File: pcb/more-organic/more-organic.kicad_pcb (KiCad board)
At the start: 2 copper layers, 156.4 x 122.7 mm, 66 parts, among them SW1 SW_Push, SW10 SW_Push, SW11 SW_Push, SW12 SW_Push, SW13 SW_Push, SW14 SW_Push, SW15 SW_Push, SW16 SW_Push, SW17 SW_Push, SW18 SW_Push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

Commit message: Follow up with new data flow on case
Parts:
- added REF**: MountingHole_2.2mm_M2_Pad_Via, MountingHole_2.2mm_M2_Pad_Via, F.Cu at (-28.5, 37.0)
- moved REF** 20.9 mm to (-38.8, 20.8)

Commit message: Routed current pcb
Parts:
- removed REF** (x6): MountingHole_2.2mm_M2_Pad_Via, MountingHole_2.2mm_M2_Pad_Via
- added ?: MountingHole_2.2mm_M2_Pad_Via, MountingHole_2.2mm_M2_Pad_Via, F.Cu at (-30.0, 39.0)
- added ?: MountingHole_2.2mm_M2_Pad_Via, MountingHole_2.2mm_M2_Pad_Via, F.Cu at (-16.0, 48.0)
- added ?: MountingHole_2.2mm_M2_Pad_Via, MountingHole_2.2mm_M2_Pad_Via, F.Cu at (-44.0, 30.0)
- added generated: MountingHole_2.2mm_M2_Pad_Via, MountingHole_2.2mm_M2_Pad_Via, F.Cu at (63.7, 61.7)
- added generated: MountingHole_2.2mm_M2_Pad_Via, MountingHole_2.2mm_M2_Pad_Via, F.Cu at (12.0, 69.2)
- added generated: MountingHole_2.2mm_M2_Pad_Via, MountingHole_2.2mm_M2_Pad_Via, F.Cu at (69.7, 5.47)
- added generated: MountingHole_2.2mm_M2_Pad_Via, MountingHole_2.2mm_M2_Pad_Via, F.Cu at (25.6, -12.5)
- moved JP1 28.4 mm to (-36.1, 24.4)
- moved JP2 28.4 mm to (-36.1, 18.6)
- moved R1 28.4 mm to (-43.3, 21.2)
- moved R2 28.4 mm to (-39.8, 21.2)
- moved SW_RESET1 12.7 mm to (-16.2, 42.8)
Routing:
- net /col4: track 0.00 -> 273.3 mm, vias 0 -> 2
- net /col2: track 0.00 -> 255.8 mm, vias 0 -> 2
- net /col3: track 0.00 -> 232.9 mm, vias 0 -> 2
- net /col1: track 0.00 -> 227.6 mm, vias 0 -> 2
- net /row0: track 0.00 -> 196.8 mm, vias 0 -> 6
- net /row2: track 0.00 -> 190.2 mm, vias 0 -> 6
- net /row3: track 0.00 -> 189.7 mm, vias 0 -> 2
- net /col0: track 0.00 -> 179.2 mm, vias 0 -> 1
- net /row1: track 0.00 -> 175.0 mm, vias 0 -> 4
- net /col5: track 152.3 -> 289.0 mm, vias 0 -> 2
- net /row4: track 0.00 -> 124.6 mm, vias 0 -> 1
- net VCC: track 12.5 -> 65.7 mm, vias 0 -> 2
- net /rst: track 0.00 -> 42.4 mm, vias 0 -> 2
- net /scl_uart: track 0.00 -> 31.6 mm
- net Net-(D24-Pad2): track 0.00 -> 25.5 mm
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- added copper zone on B.Cu, net GND
- added copper zone on F.Cu, net GND
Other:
- outline, holes or cut-outs redrawn
- net class Supply added: clearance 0.5, trace_width 0.5, via_dia 0.8, via_drill 0.4

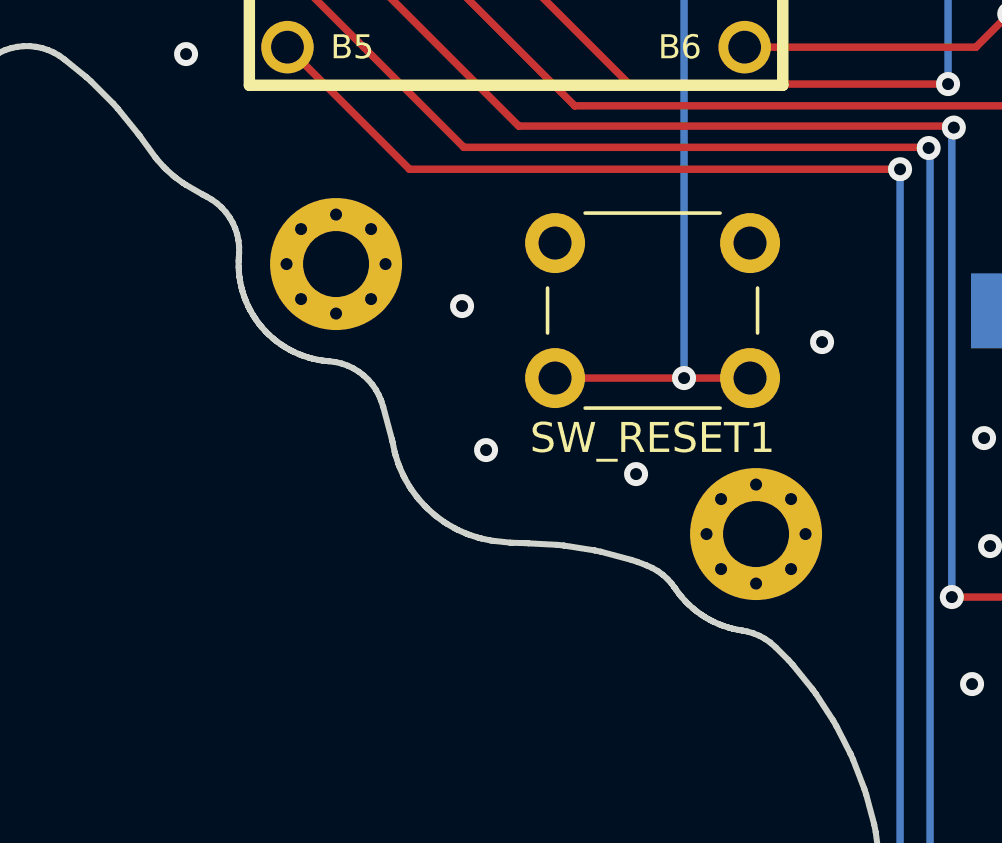
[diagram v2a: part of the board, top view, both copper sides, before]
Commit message: Add cover and plate makefile placer commands
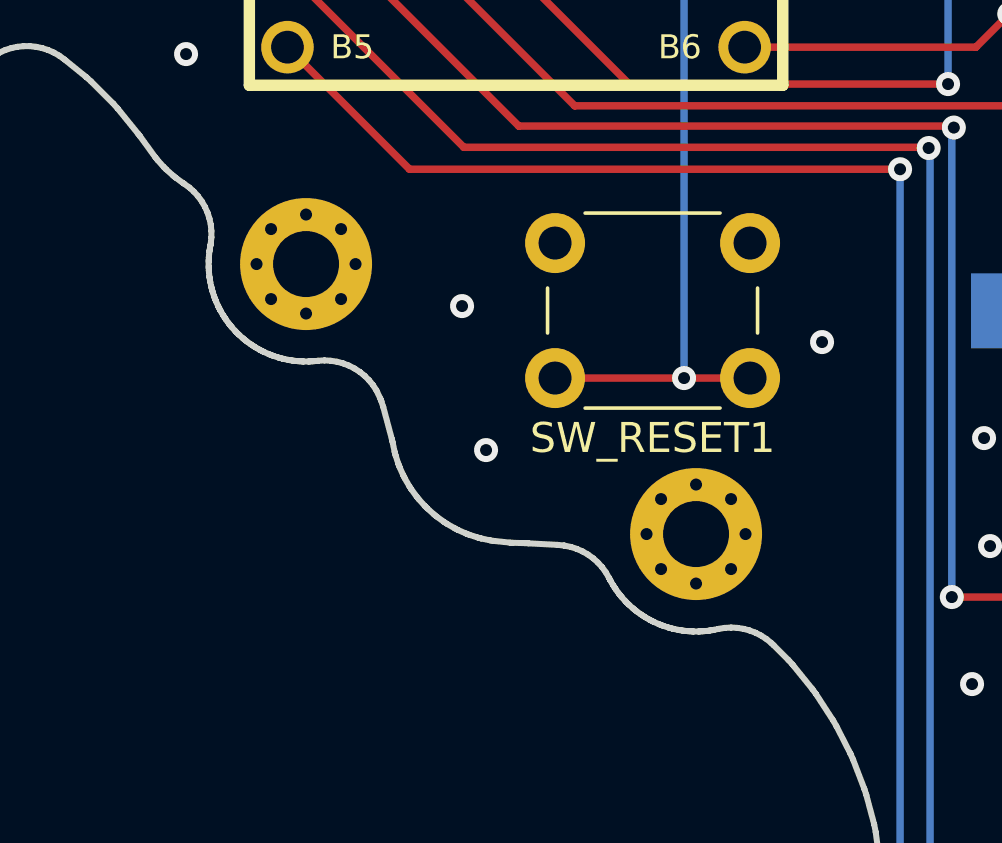
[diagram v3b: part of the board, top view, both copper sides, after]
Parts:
- removed the ? at (-30.0, 39.0)
- removed the ? at (-16.0, 48.0)
- added ?: MountingHole_2.2mm_M2_Pad_Via, MountingHole_2.2mm_M2_Pad_Via, F.Cu at (-31.0, 39.0)
- added ?: MountingHole_2.2mm_M2_Pad_Via, MountingHole_2.2mm_M2_Pad_Via, F.Cu at (-18.0, 48.0)
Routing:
- net GND: vias 171 -> 170
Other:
- outline, holes or cut-outs redrawn
